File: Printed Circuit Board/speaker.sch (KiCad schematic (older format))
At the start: 7 parts, among them J2 Conn_01x05_Male, J3 Conn_01x02_Male

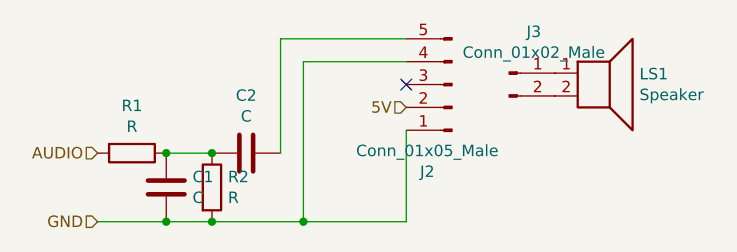
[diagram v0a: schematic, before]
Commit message: PCB: physical board prototype
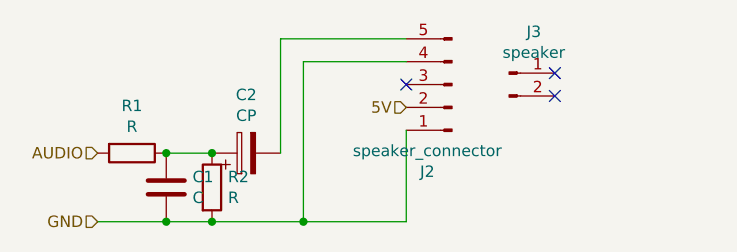
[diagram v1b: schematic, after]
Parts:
- removed C2: C, symbol Device:C
- removed LS1: Speaker, symbol Device:Speaker
- added C2: CP, Capacitor_THT:C_Radial_D6.3mm_H5.0mm_P2.50mm, symbol Device:CP
- C1: footprint (none) -> Capacitor_THT:C_Disc_D4.7mm_W2.5mm_P5.00mm
- J2: value Conn_01x05_Male -> speaker_connector; footprint (none) -> Connector_PinHeader_2.54mm:PinHeader_1x05_P2.54mm_Vertical
- J3: value Conn_01x02_Male -> speaker; footprint (none) -> Connector_PinHeader_2.54mm:PinHeader_1x02_P2.54mm_Vertical
- R1: footprint (none) -> Resistor_SMD:R_1206_3216Metric_Pad1.30x1.75mm_HandSolder
- R2: footprint (none) -> Resistor_SMD:R_1206_3216Metric
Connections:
- net at J2.5 (Pin_5): now also C2.2
- net at C1.1, R1.1, R2.1: now also C2.1
- no-connect marks 1 -> 3
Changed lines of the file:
@@
 Comment4 ""
 $EndDescr
-$Comp
-L Connector:Conn_01x02_Male J?
-U 1 1 603AD9B8
-P 6550 3500
-AR Path="/603AD9B8" Ref="J?"  Part="1"
-AR Path="/603AA30A/603AD9B8" Ref="J3"  Part="1"
-F 0 "J3" H 6658 3681 50  0000 C CNN
-F 1 "Conn_01x02_Male" H 6658 3590 50  0000 C CNN
-F 2 "" H 6550 3500 50  0001 C CNN
-F 3 "~" H 6550 3500 50  0001 C CNN
-	1    6550 3500
-	1    0    0    -1
-$EndComp
 Connection ~ 5650 4150
 Connection ~ 5250 4150
@@
 Wire Wire Line
 	5550 3850 5550 3350
-Connection ~ 5250 3850
-$Comp
-L Device:C C?
-U 1 1 603AD9C8
-P 5400 3850
-AR Path="/603AD9C8" Ref="C?"  Part="1"
-AR Path="/603AA30A/603AD9C8" Ref="C2"  Part="1"
-F 0 "C2" V 5148 3850 50  0000 C CNN
-F 1 "C" V 5239 3850 50  0000 C CNN
-F 2 "" H 5438 3700 50  0001 C CNN
-F 3 "~" H 5400 3850 50  0001 C CNN
-	1    5400 3850
-	0    1    1    0
-$EndComp
 Wire Wire Line
 	5250 4150 5050 4150
@@
 F 0 "C1" H 5165 4046 50  0000 L CNN
 F 1 "C" H 5165 3955 50  0000 L CNN
-F 2 "" H 5088 3850 50  0001 C CNN
+F 2 "Capacitor_THT:C_Disc_D4.7mm_W2.5mm_P5.00mm" H 5088 3850 50  0001 C CNN
 F 3 "~" H 5050 4000 50  0001 C CNN
 	1    5050 4000
@@
 F 0 "R2" H 5320 4046 50  0000 L CNN
 F 1 "R" H 5320 3955 50  0000 L CNN
-F 2 "" V 5180 4000 50  0001 C CNN
+F 2 "Resistor_SMD:R_1206_3216Metric" V 5180 4000 50  0001 C CNN
 F 3 "~" H 5250 4000 50  0001 C CNN
 	1    5250 4000
@@
 F 0 "R1" V 4693 3850 50  0000 C CNN
 F 1 "R" V 4784 3850 50  0000 C CNN
-F 2 "" V 4830 3850 50  0001 C CNN
+F 2 "Resistor_SMD:R_1206_3216Metric_Pad1.30x1.75mm_HandSolder" V 4830 3850 50  0001 C CNN
 F 3 "~" H 4900 3850 50  0001 C CNN
 	1    4900 3850
@@
 AR Path="/603AA30A/603AD9E3" Ref="J2"  Part="1"
 F 0 "J2" H 6408 3931 50  0000 C CNN
-F 1 "Conn_01x05_Male" H 6408 3840 50  0000 C CNN
-F 2 "" H 6300 3550 50  0001 C CNN
+F 1 "speaker_connector" H 6408 3840 50  0000 C CNN
+F 2 "Connector_PinHeader_2.54mm:PinHeader_1x05_P2.54mm_Vertical" H 6300 3550 50  0001 C CNN
 F 3 "~" H 6300 3550 50  0001 C CNN
 	1    6300 3550
 	-1   0    0    1
-$EndComp
-$Comp
-L Device:Speaker LS?
-U 1 1 603AD9E9
-P 6950 3500
-AR Path="/603AD9E9" Ref="LS?"  Part="1"
-AR Path="/603AA30A/603AD9E9" Ref="LS1"  Part="1"
-F 0 "LS1" H 7120 3496 50  0000 L CNN
-F 1 "Speaker" H 7120 3405 50  0000 L CNN
-F 2 "" H 6950 3300 50  0001 C CNN
-F 3 "~" H 6940 3450 50  0001 C CNN
-	1    6950 3500
-	1    0    0    -1
 $EndComp
 Wire Wire Line
@@
 Text HLabel 4750 4150 0    50   Input ~ 0
 GND
+$Comp
+L Device:CP C2
+U 1 1 6032FD6D
+P 5400 3850
+F 0 "C2" V 5655 3850 50  0000 C CNN
+F 1 "CP" V 5564 3850 50  0000 C CNN
+F 2 "Capacitor_THT:C_Radial_D6.3mm_H5.0mm_P2.50mm" H 5438 3700 50  0001 C CNN
+F 3 "~" H 5400 3850 50  0001 C CNN
+	1    5400 3850
+	0    -1   -1   0
+$EndComp
+Connection ~ 5250 3850
+$Comp
+L Connector:Conn_01x02_Male J?
+U 1 1 603AD9B8
+P 6550 3500
+AR Path="/603AD9B8" Ref="J?"  Part="1"
+AR Path="/603AA30A/603AD9B8" Ref="J3"  Part="1"
+F 0 "J3" H 6658 3681 50  0000 C CNN
+F 1 "speaker" H 6658 3590 50  0000 C CNN
+F 2 "Connector_PinHeader_2.54mm:PinHeader_1x02_P2.54mm_Vertical" H 6550 3500 50  0001 C CNN
+F 3 "~" H 6550 3500 50  0001 C CNN
+	1    6550 3500
+	1    0    0    -1
+$EndComp
+NoConn ~ 6750 3500
+NoConn ~ 6750 3600
 $EndSCHEMATC

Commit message: PCB physical board
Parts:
- J2: value speaker_connector -> speaker connector
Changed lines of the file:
@@
 AR Path="/603AA30A/603AD9E3" Ref="J2"  Part="1"
 F 0 "J2" H 6408 3931 50  0000 C CNN
-F 1 "speaker_connector" H 6408 3840 50  0000 C CNN
+F 1 "speaker connector" H 6408 3840 50  0000 C CNN
 F 2 "Connector_PinHeader_2.54mm:PinHeader_1x05_P2.54mm_Vertical" H 6300 3550 50  0001 C CNN
 F 3 "~" H 6300 3550 50  0001 C CNN
